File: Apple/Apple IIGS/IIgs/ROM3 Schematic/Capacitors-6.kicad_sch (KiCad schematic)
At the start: 98 parts

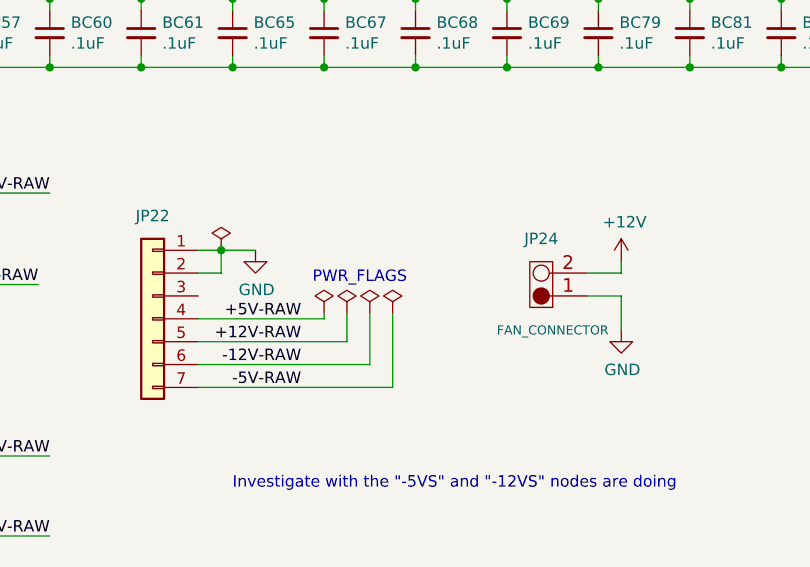
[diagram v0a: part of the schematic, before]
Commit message: 399 ERC, Rescue symbol clean-up
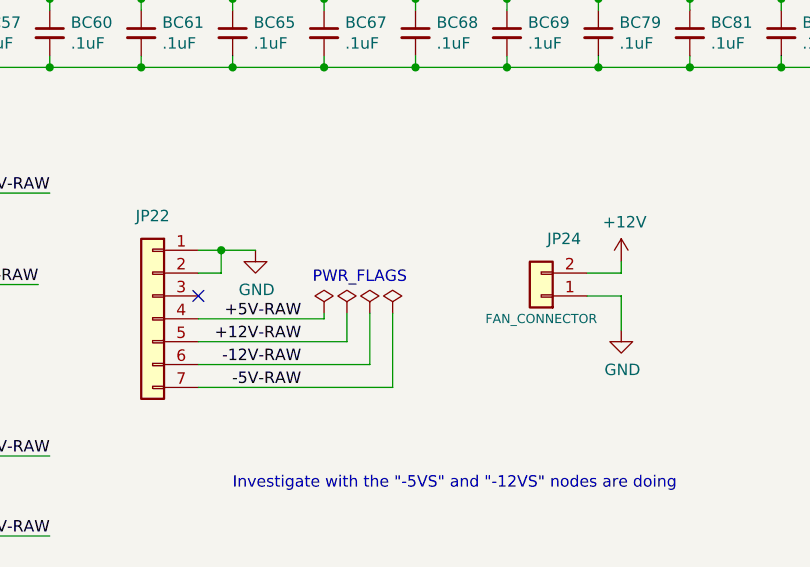
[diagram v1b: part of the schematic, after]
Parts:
- C42, C43, C44, C45, C46, SC13, SC20: symbol IIgs-Schematic-rescue:CP_Small-Device -> Device:C_Polarized_Small
- JP24: symbol IIgs-Schematic-rescue:M02-freetronics_schematic-IIgs-Schematic-rescue -> Connector_Generic:Conn_01x02
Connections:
- no-connect marks 0 -> 1
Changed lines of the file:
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@@
   (junction (at 101.6 69.85) (diameter 0) (color 0 0 0 0)
   )
+  (no_connect (at 179.07 148.59))
   (wire (pts (xy 71.12 62.23) (xy 60.96 62.23))
     (stroke (width 0) (type default) (color 0 0 0 0))
@@
     (pin "2")
   )
-  (symbol (lib_id "IIgs-Schematic-rescue:CP_Small-Device") (at 46.99 115.57 180) (unit 1)
+  (symbol (lib_id "Device:C_Polarized_Small") (at 46.99 115.57 180) (unit 1)
     (in_bom yes) (on_board yes)
     (property "Reference" "SC13" (id 0) (at 44.6532 116.7384 0)
@@
     (pin "2")
   )
-  (symbol (lib_id "IIgs-Schematic-rescue:CP_Small-Device") (at 46.99 135.89 180) (unit 1)
+  (symbol (lib_id "Device:C_Polarized_Small") (at 46.99 135.89 180) (unit 1)
     (in_bom yes) (on_board yes)
     (property "Reference" "SC20" (id 0) (at 44.6532 137.0584 0)
@@
     (pin "1")
   )
-  (symbol (lib_id "IIgs-Schematic-rescue:CP_Small-Device") (at 118.11 137.16 90) (unit 1)
+  (symbol (lib_id "Device:C_Polarized_Small") (at 118.11 137.16 90) (unit 1)
     (in_bom yes) (on_board yes)
     (property "Reference" "C42" (id 0) (at 119.38 140.97 90)
@@
     (pin "2")
   )
-  (symbol (lib_id "IIgs-Schematic-rescue:CP_Small-Device") (at 118.11 156.21 270) (unit 1)
+  (symbol (lib_id "Device:C_Polarized_Small") (at 118.11 156.21 270) (unit 1)
     (in_bom yes) (on_board yes)
     (property "Reference" "C44" (id 0) (at 116.84 153.67 90)
@@
     (pin "2")
   )
-  (symbol (lib_id "IIgs-Schematic-rescue:CP_Small-Device") (at 129.54 147.32 270) (unit 1)
+  (symbol (lib_id "Device:C_Polarized_Small") (at 129.54 147.32 270) (unit 1)
     (in_bom yes) (on_board yes)
     (property "Reference" "C43" (id 0) (at 128.27 144.78 90)
@@
     (pin "2")
   )
-  (symbol (lib_id "IIgs-Schematic-rescue:CP_Small-Device") (at 130.81 175.26 270) (unit 1)
+  (symbol (lib_id "Device:C_Polarized_Small") (at 130.81 175.26 270) (unit 1)
     (in_bom yes) (on_board yes)
     (property "Reference" "C46" (id 0) (at 128.27 172.72 90)
@@
     (pin "2")
   )
-  (symbol (lib_id "IIgs-Schematic-rescue:CP_Small-Device") (at 118.11 166.37 90) (unit 1)
+  (symbol (lib_id "Device:C_Polarized_Small") (at 118.11 166.37 90) (unit 1)
     (in_bom yes) (on_board yes)
     (property "Reference" "C45" (id 0) (at 120.65 163.83 90)
@@
     (pin "1")
   )
-  (symbol (lib_id "IIgs-Schematic-rescue:M02-freetronics_schematic-IIgs-Schematic-rescue") (at 214.63 148.59 180) (unit 1)
+  (symbol (lib_id "Connector_Generic:Conn_01x02") (at 217.17 148.59 180) (unit 1)
     (in_bom yes) (on_board yes)
-    (property "Reference" "JP24" (id 0) (at 217.17 142.24 0))
-    (property "Value" "FAN_CONNECTOR" (id 1) (at 218.44 152.4 0)
+    (property "Reference" "JP24" (id 0) (at 219.71 142.24 0))
+    (property "Value" "FAN_CONNECTOR" (id 1) (at 217.17 151.13 0)
       (effects (font (size 1.016 1.016)))
     )
-    (property "Footprint" "" (id 2) (at 214.63 148.59 0)
-      (effects (font (size 1.524 1.524)))
+    (property "Footprint" "" (id 2) (at 217.17 148.59 0)
+      (effects (font (size 1.27 1.27)) hide)
     )
-    (property "Datasheet" "" (id 3) (at 214.63 148.59 0)
-      (effects (font (size 1.524 1.524)))
+    (property "Datasheet" "~" (id 3) (at 217.17 148.59 0)
+      (effects (font (size 1.27 1.27)) hide)
     )
     (pin "1")
@@
       (effects (font (size 1.27 1.27)) hide)
     )
-    (pin "1")
-  )
-  (symbol (lib_id "power:PWR_FLAG") (at 181.61 143.51 0) (unit 1)
-    (in_bom yes) (on_board yes) (fields_autoplaced)
-    (property "Reference" "#FLG0105" (id 0) (at 181.61 141.605 0)
-      (effects (font (size 1.27 1.27)) hide)
-    )
-    (property "Value" "PWR_FLAG" (id 1) (at 181.61 137.795 0)
-      (effects (font (size 1.27 1.27)) hide)
-    )
-    (property "Footprint" "" (id 2) (at 181.61 143.51 0)
-      (effects (font (size 1.27 1.27)) hide)
-    )
-    (property "Datasheet" "~" (id 3) (at 181.61 143.51 0)
-      (effects (font (size 1.27 1.27)) hide)
-    )

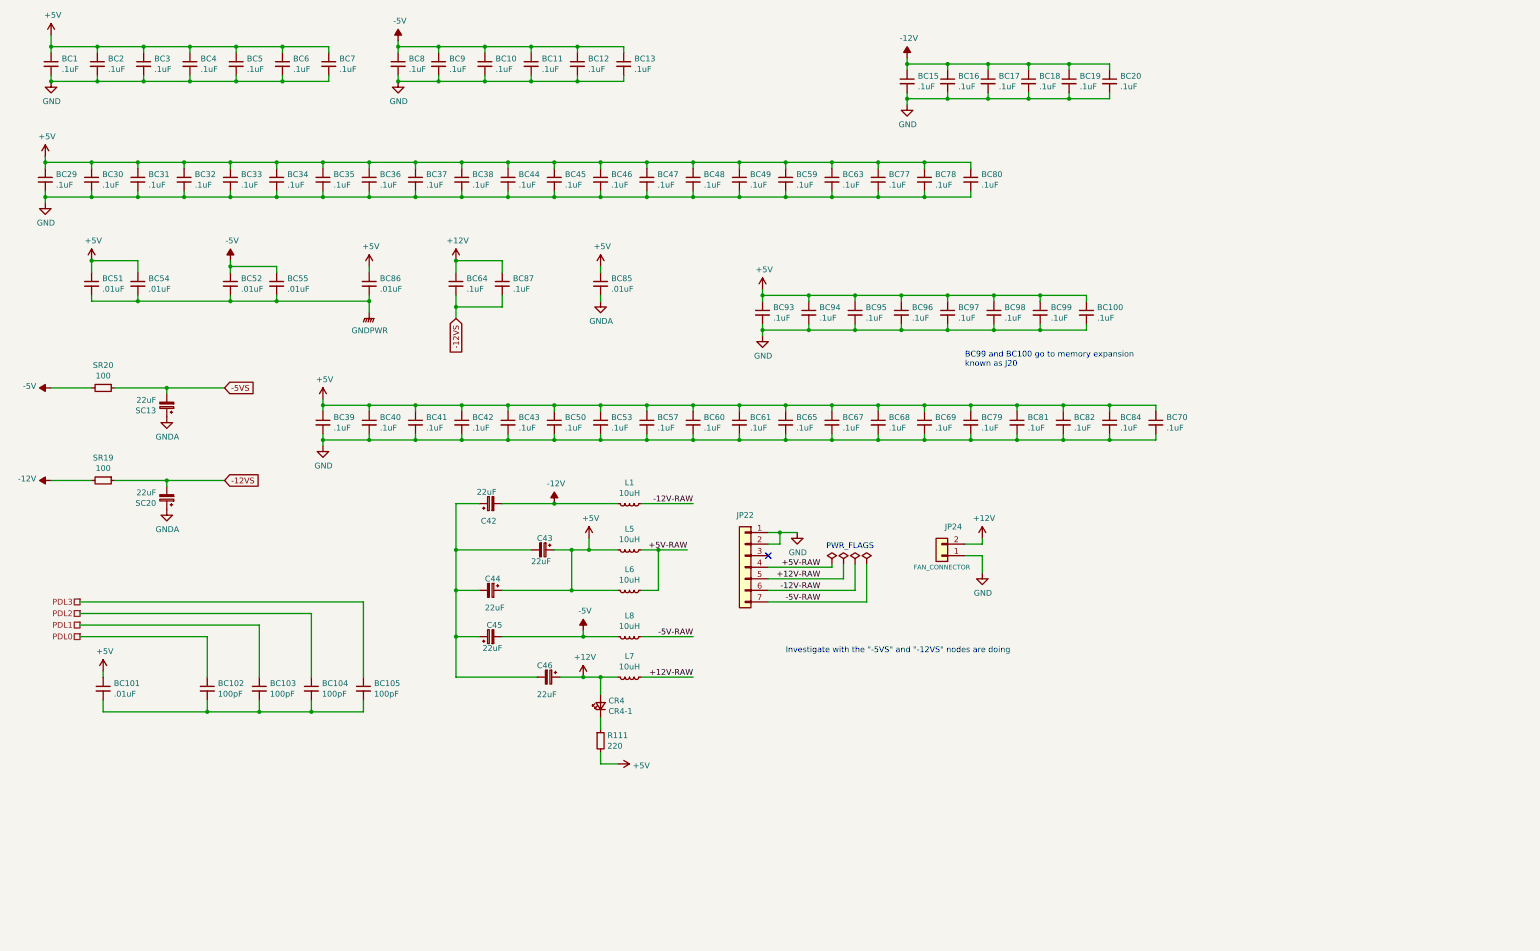
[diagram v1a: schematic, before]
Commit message: 0 ERC Errors AND Warnings. Whew. ICs updated with correct pin assignments and many (many) other fixes.
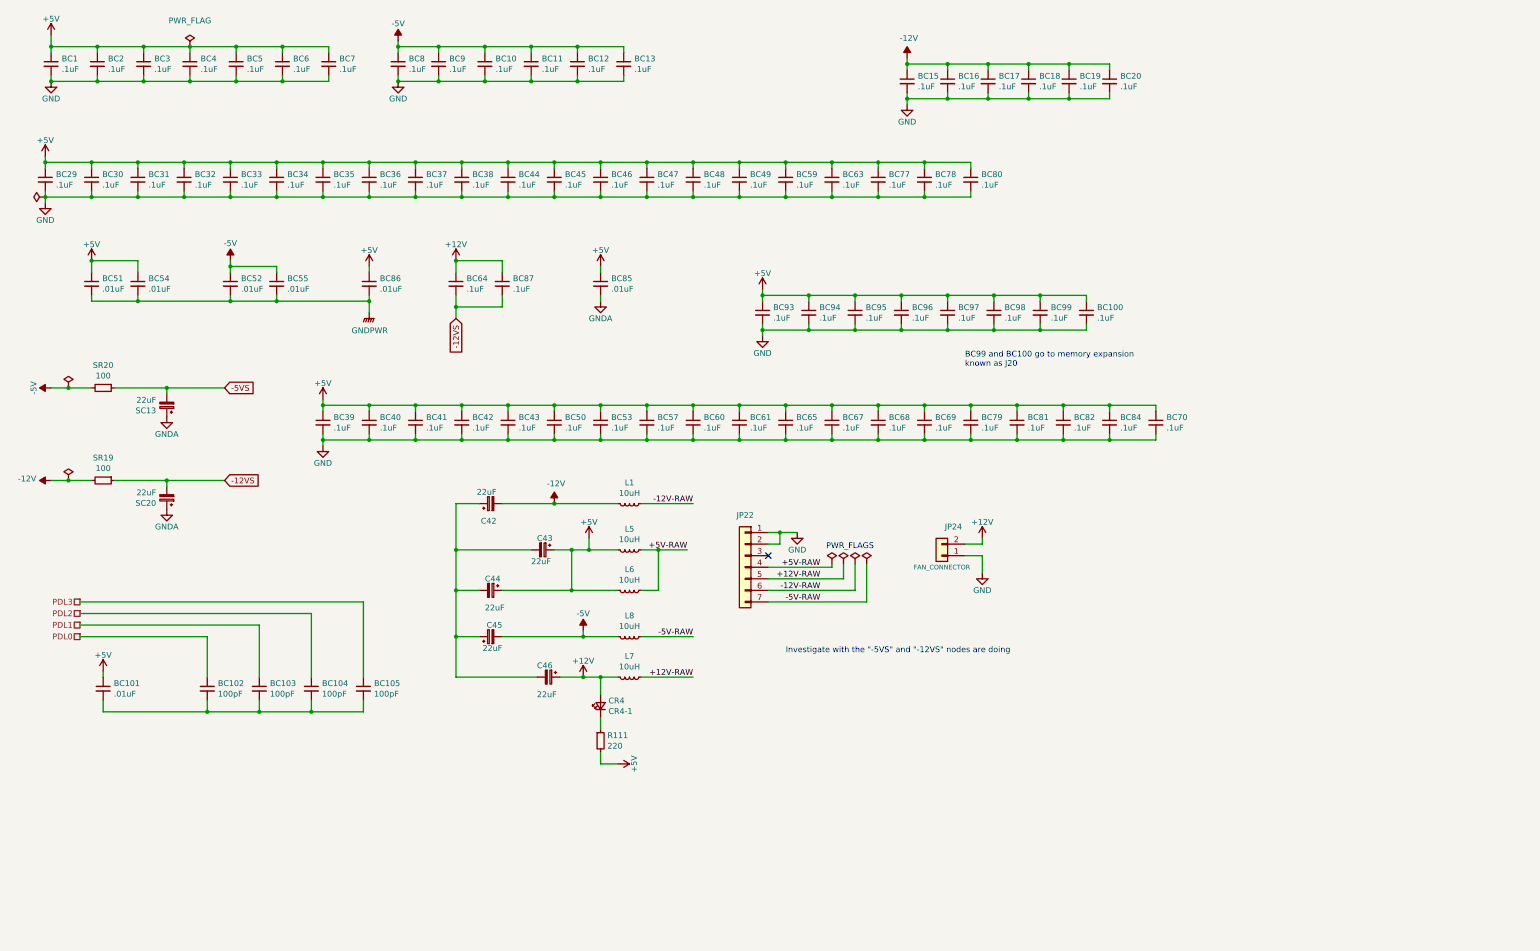
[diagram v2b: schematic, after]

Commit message: Formatting clean-up
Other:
- moved on the sheet: BC1, BC10, BC100, BC101, BC102, BC103, BC104, BC105, BC11, BC12, BC13, BC15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

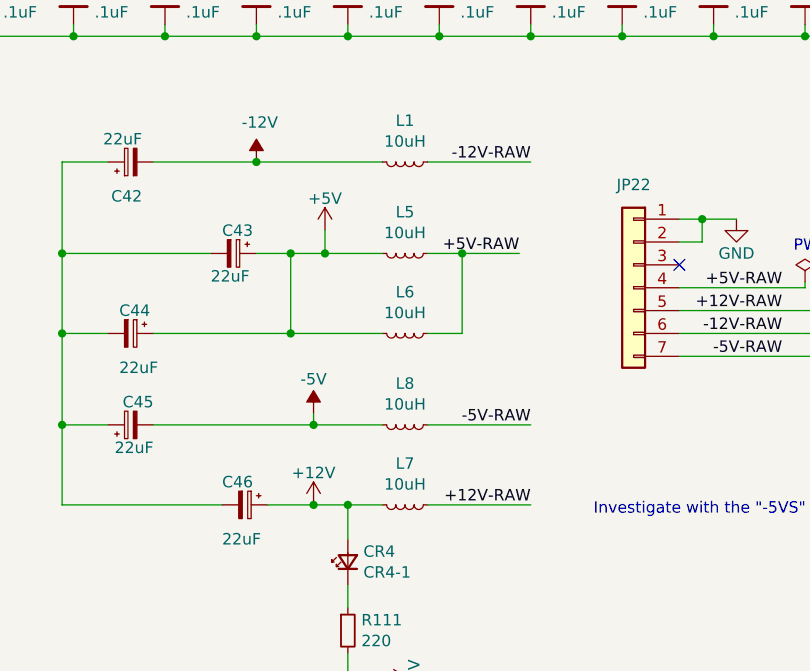
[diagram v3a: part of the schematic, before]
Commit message: Cleaned up v7 ERCs and removed v5 files
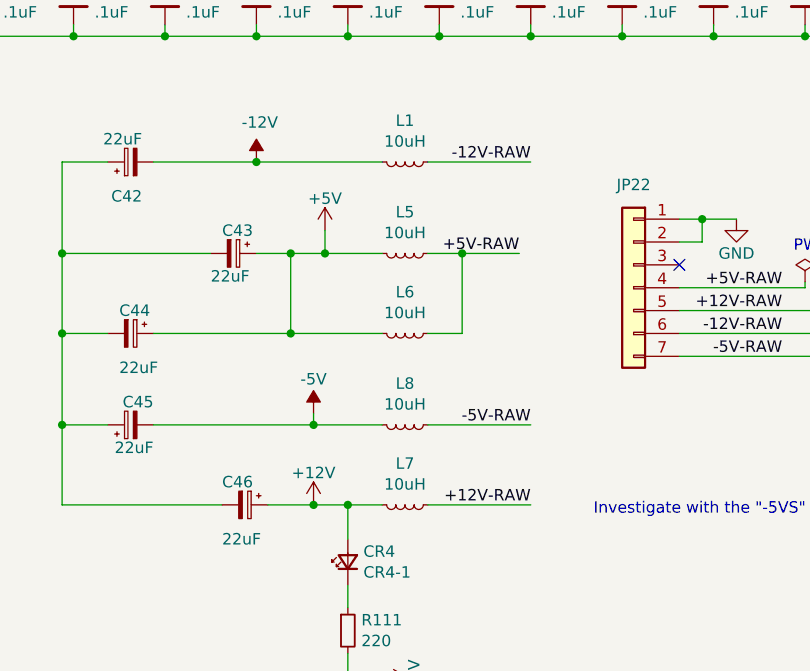
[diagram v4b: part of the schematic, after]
